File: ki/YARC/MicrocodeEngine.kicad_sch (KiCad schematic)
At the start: 12 parts, among them U32 74HC245, U33 AS6C6264, U34 74LS574, U35 74HC245, U36 AS6C6264, U37 74LS574, U38 74HC245, U39 AS6C6264, U40 74LS574, U41 74HC245, U42 AS6C6264, U43 74LS574

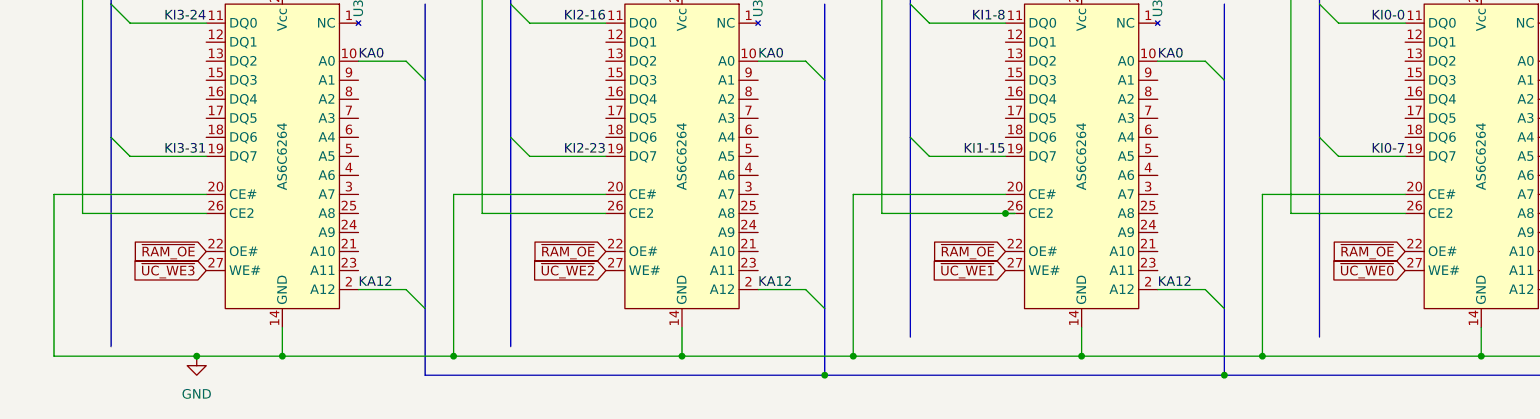
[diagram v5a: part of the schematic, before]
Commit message: Large commit. Document two hardware changes to microcode controls. Adapt Nano firmware to these changes. Significantly simplify initialization logic and make it more consistent about reset.
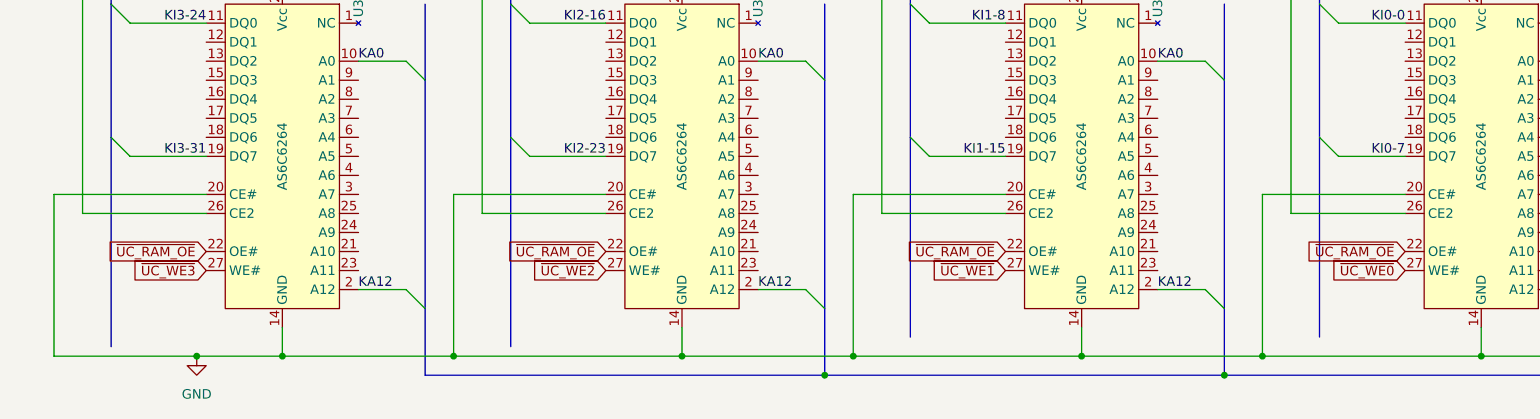
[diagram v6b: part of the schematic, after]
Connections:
- net ~{RAM_OE} renamed ~{UC_RAM_OE}
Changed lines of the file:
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@@
   (junction (at 205.74 165.1) (diameter 0) (color 0 0 0 0)
   )
-  (junction (at 142.24 146.05) (diameter 0) (color 0 0 0 0)
-  )
   (junction (at 45.72 165.1) (diameter 0) (color 0 0 0 0)
   )
@@
     (stroke (width 0) (type default) (color 0 0 0 0))
   )
+  (wire (pts (xy 125.73 146.05) (xy 142.24 146.05))
+    (stroke (width 0) (type default) (color 0 0 0 0))
+  )
   (bus (pts (xy 184.15 62.23) (xy 184.15 72.39))
     (stroke (width 0) (type default) (color 0 0 0 0))
@@
     (stroke (width 0) (type default) (color 0 0 0 0))
   )
-  (wire (pts (xy 142.24 146.05) (xy 125.73 146.05))
-    (stroke (width 0) (type default) (color 0 0 0 0))
-  )
   (bus (pts (xy 129.54 62.23) (xy 142.24 62.23))
     (stroke (width 0) (type default) (color 0 0 0 0))
@@
     (stroke (width 0) (type default) (color 0 0 0 0))
   )
-  (wire (pts (xy 143.51 146.05) (xy 142.24 146.05))
-    (stroke (width 0) (type default) (color 0 0 0 0))
-  )
   (wire (pts (xy 152.4 67.31) (xy 99.06 67.31))
     (stroke (width 0) (type default) (color 0 0 0 0))
@@
     )
   )
-  (global_label "~{RAM_OE}" (shape input) (at 35.56 151.13 180) (fields_autoplaced)
-    (effects (font (size 1.27 1.27)) (justify right))
-    (property "Intersheet References" "${INTERSHEET_REFS}" (id 0) (at 25.8898 151.0506 0)
-      (effects (font (size 1.27 1.27)) (justify right) hide)
-    )
-  )
-  (global_label "~{RAM_OE}" (shape input) (at 88.9 151.13 180) (fields_autoplaced)
-    (effects (font (size 1.27 1.27)) (justify right))
-    (property "Intersheet References" "${INTERSHEET_REFS}" (id 0) (at 79.2298 151.0506 0)
+  (global_label "~{UC_RAM_OE}" (shape input) (at 35.56 151.13 180) (fields_autoplaced)
+    (effects (font (size 1.27 1.27)) (justify right))
+    (property "Intersheet References" "${INTERSHEET_REFS}" (id 0) (at 22.3217 151.2094 0)
+      (effects (font (size 1.27 1.27)) (justify right) hide)
+    )
+  )
+  (global_label "~{UC_RAM_OE}" (shape input) (at 195.58 151.13 180) (fields_autoplaced)
+    (effects (font (size 1.27 1.27)) (justify right))
+    (property "Intersheet References" "${INTERSHEET_REFS}" (id 0) (at 182.3417 151.2094 0)
       (effects (font (size 1.27 1.27)) (justify right) hide)
     )
@@
     )
   )
-  (global_label "~{RAM_OE}" (shape input) (at 142.24 151.13 180) (fields_autoplaced)
-    (effects (font (size 1.27 1.27)) (justify right))
-    (property "Intersheet References" "${INTERSHEET_REFS}" (id 0) (at 132.5698 151.0506 0)
-      (effects (font (size 1.27 1.27)) (justify right) hide)
-    )
-  )
-  (global_label "~{RAM_OE}" (shape input) (at 195.58 151.13 180) (fields_autoplaced)
-    (effects (font (size 1.27 1.27)) (justify right))
-    (property "Intersheet References" "${INTERSHEET_REFS}" (id 0) (at 185.9098 151.0506 0)
+  (global_label "~{UC_RAM_OE}" (shape input) (at 88.9 151.13 180) (fields_autoplaced)
+    (effects (font (size 1.27 1.27)) (justify right))
+    (property "Intersheet References" "${INTERSHEET_REFS}" (id 0) (at 75.6617 151.2094 0)
       (effects (font (size 1.27 1.27)) (justify right) hide)
     )
@@
       (effects (font (size 1.27 1.27)) (justify right) hide)
     )
+  )
+  (global_label "~{UC_RAM_OE}" (shape input) (at 142.24 151.13 180) (fields_autoplaced)
+    (effects (font (size 1.27 1.27)) (justify right))
+    (property "Intersheet References" "${INTERSHEET_REFS}" (id 0) (at 129.0017 151.2094 0)
+      (effects (font (size 1.27 1.27)) (justify right) hide)
+    )

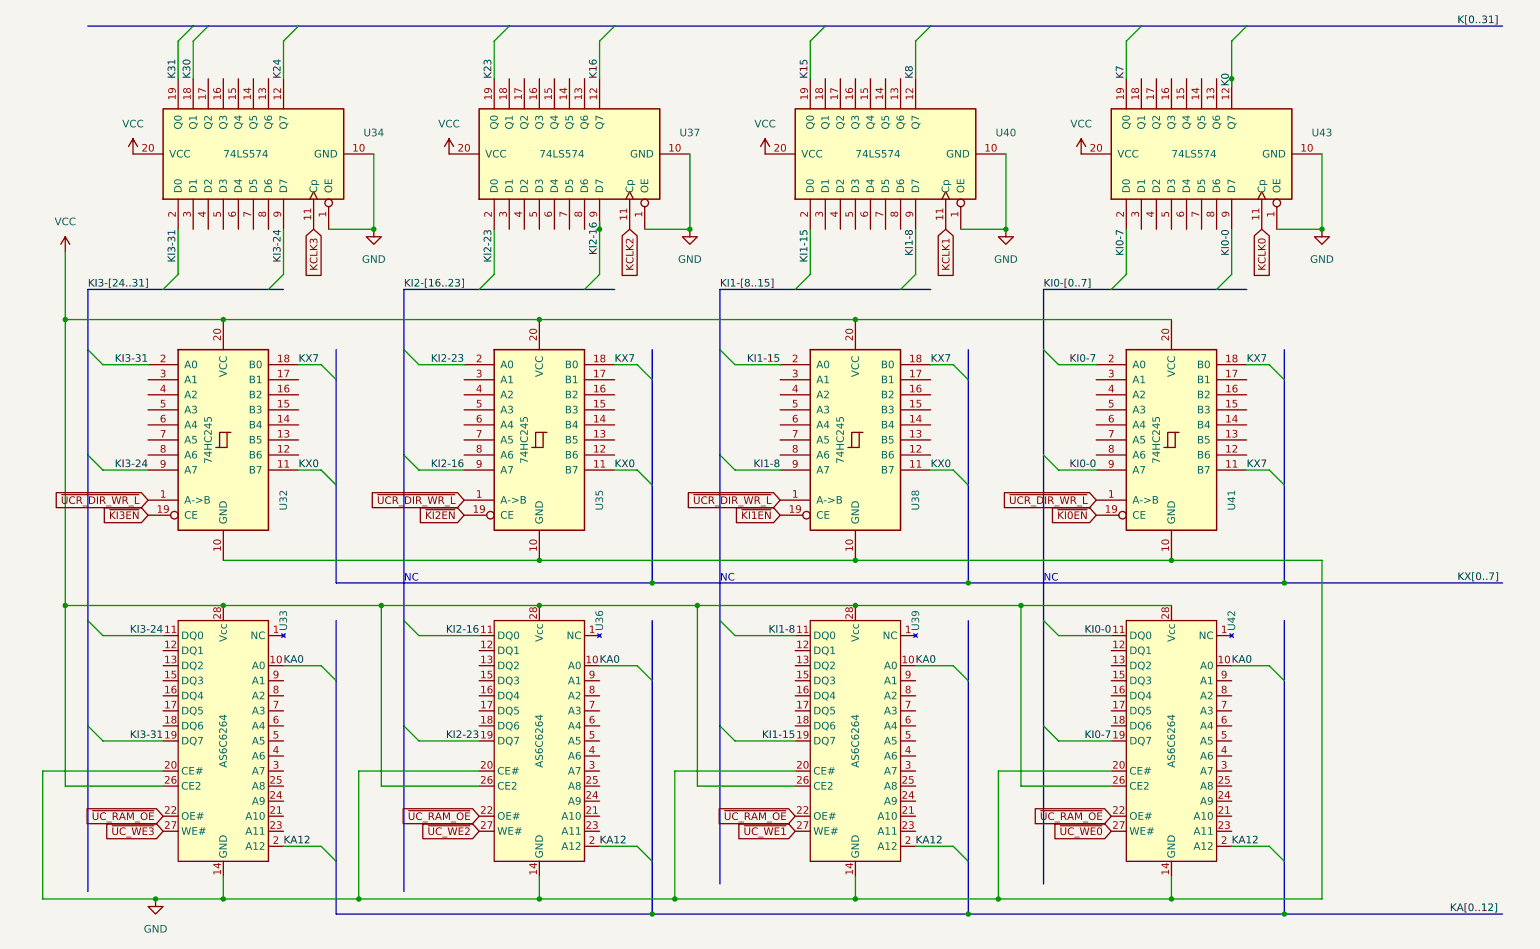
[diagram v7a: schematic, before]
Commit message: Removed about 2/3 of 2300+ errors from the ERC
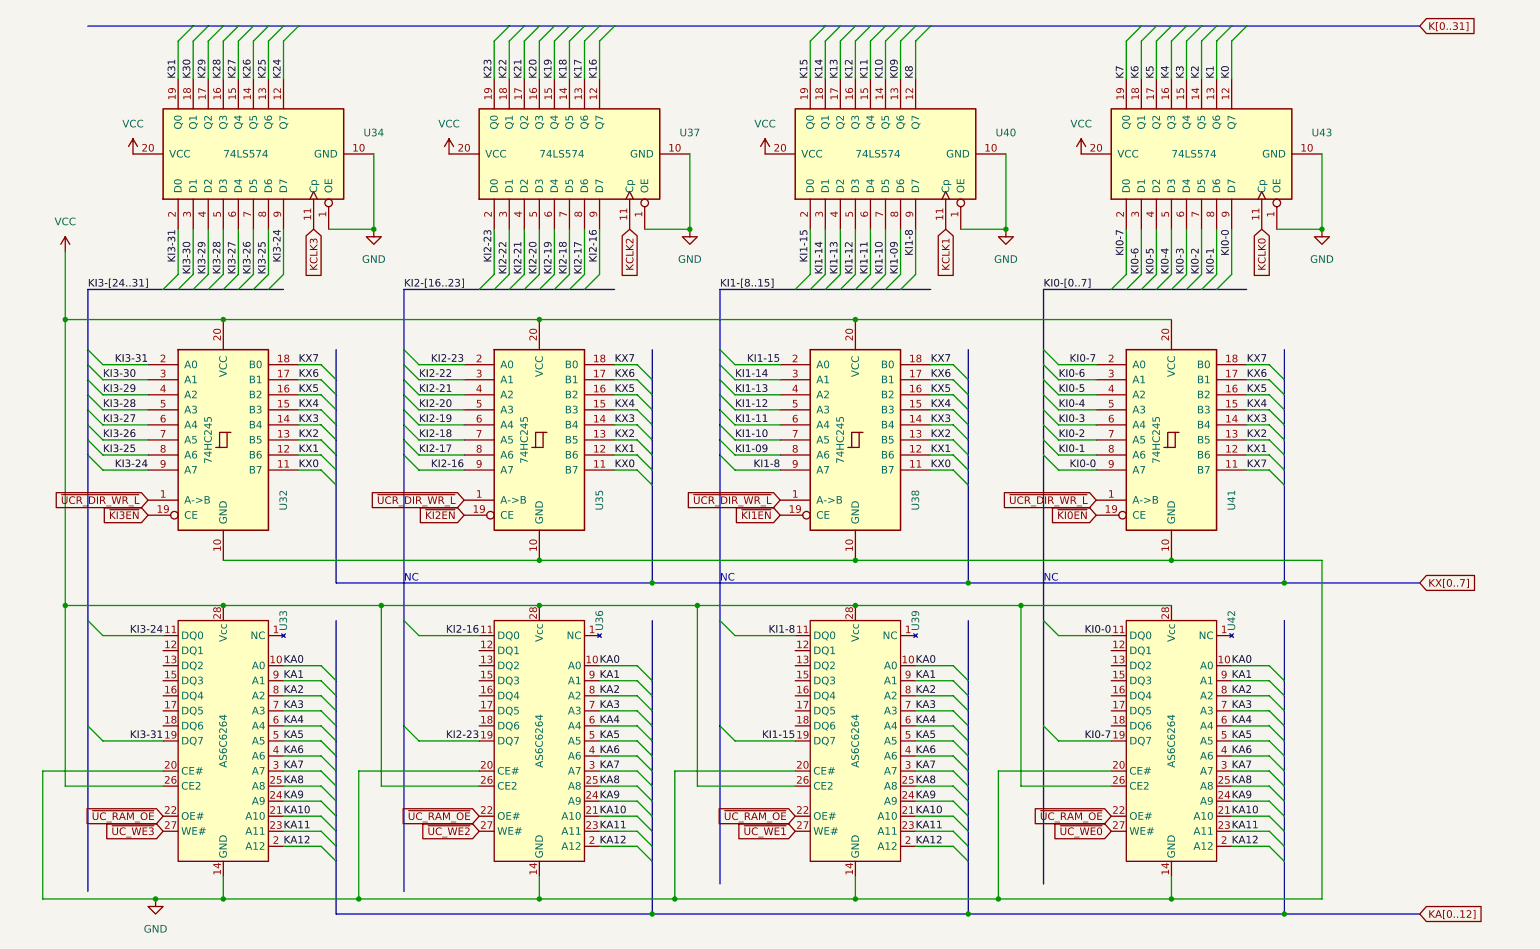
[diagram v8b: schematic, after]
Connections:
- net K17: now reaches U37.13 (Q6)
- net K18: now reaches U37.14 (Q5)
- net K19: now reaches U37.15 (Q4)
- net K20: now reaches U37.16 (Q3)
- net K21: now reaches U37.17 (Q2)
- net K22: now reaches U37.18 (Q1)
- net KI2-22: now reaches U37.3 (D1)
- net KI2-22: now also U35.3 (A1)
- net KI2-21: now reaches U37.4 (D2)
- net KI2-21: now also U35.4 (A2)
- net KI2-20: now reaches U37.5 (D3)
- net KI2-20: now also U35.5 (A3)
- net KI2-19: now reaches U37.6 (D4)
- net KI2-19: now also U35.6 (A4)
- net KI2-18: now reaches U37.7 (D5)
- net KI2-18: now also U35.7 (A5)
- net KI2-17: now reaches U37.8 (D6)
- net KI2-17: now also U35.8 (A6)
- net KA10: now reaches U36.21 (A10)
- net KA10: now also U33.21 (A10), U39.21 (A10), U42.21 (A10)
- net KA11: now reaches U36.23 (A11)
- net KA11: now also U33.23 (A11), U39.23 (A11), U42.23 (A11)
- net KA9: now reaches U36.24 (A9)
- net KA9: now also U33.24 (A9), U39.24 (A9), U42.24 (A9)
- net KA8: now reaches U36.25 (A8)
- net KA8: now also U33.25 (A8), U39.25 (A8), U42.25 (A8)
- net KA7: now reaches U36.3 (A7)
- net KA7: now also U33.3 (A7), U39.3 (A7), U42.3 (A7)
- net KA6: now reaches U36.4 (A6)
- net KA6: now also U33.4 (A6), U39.4 (A6), U42.4 (A6)
- net KA5: now reaches U36.5 (A5)
- net KA5: now also U33.5 (A5), U39.5 (A5), U42.5 (A5)
- net KA4: now reaches U36.6 (A4)
- net KA4: now also U33.6 (A4), U39.6 (A4), U42.6 (A4)
- net KA3: now reaches U36.7 (A3)
- net KA3: now also U33.7 (A3), U39.7 (A3), U42.7 (A3)
- net KA2: now reaches U36.8 (A2)
- net KA2: now also U33.8 (A2), U39.8 (A2), U42.8 (A2)
- net KA1: now reaches U36.9 (A1)
- net KA1: now also U33.9 (A1), U39.9 (A1), U42.9 (A1)
- net KX1: now reaches U32.12 (B6)
- net KX1: now also U35.12 (B6), U38.12 (B6), U41.12 (B6)
- net KX2: now reaches U32.13 (B5)
- net KX2: now also U35.13 (B5), U38.13 (B5), U41.13 (B5)
- net KX3: now reaches U32.14 (B4)
- net KX3: now also U35.14 (B4), U38.14 (B4), U41.14 (B4)
- net KX4: now reaches U32.15 (B3)
- net KX4: now also U35.15 (B3), U38.15 (B3), U41.15 (B3)
- net KX5: now reaches U32.16 (B2)
- net KX5: now also U35.16 (B2), U38.16 (B2), U41.16 (B2)
- net KX6: now reaches U32.17 (B1)
- net KX6: now also U35.17 (B1), U38.17 (B1), U41.17 (B1)
- net KI3-30: now reaches U32.3 (A1)
- net KI3-30: now also U34.3 (D1)
- net KI3-29: now reaches U32.4 (A2)
- net KI3-29: now also U34.4 (D2)
- net KI3-28: now reaches U32.5 (A3)
- net KI3-28: now also U34.5 (D3)
- net KI3-27: now reaches U32.6 (A4)
- net KI3-27: now also U34.6 (D4)
- net KI3-26: now reaches U32.7 (A5)
- net KI3-26: now also U34.7 (D5)
- net KI3-25: now reaches U32.8 (A6)
- net KI3-25: now also U34.8 (D6)
- net K1: now reaches U43.13 (Q6)
- net K2: now reaches U43.14 (Q5)
- net K3: now reaches U43.15 (Q4)
- net K4: now reaches U43.16 (Q3)
- net K5: now reaches U43.17 (Q2)
- net K6: now reaches U43.18 (Q1)
- net KI0-6: now reaches U43.3 (D1)
- net KI0-6: now also U41.3 (A1)
- net KI0-5: now reaches U43.4 (D2)
- net KI0-5: now also U41.4 (A2)
- net KI0-4: now reaches U43.5 (D3)
- net KI0-4: now also U41.5 (A3)
- net KI0-3: now reaches U43.6 (D4)
- net KI0-3: now also U41.6 (A4)
- net KI0-2: now reaches U43.7 (D5)
- net KI0-2: now also U41.7 (A5)
- net KI0-1: now reaches U43.8 (D6)
- net KI0-1: now also U41.8 (A6)
- net K25: now reaches U34.13 (Q6)
- net K26: now reaches U34.14 (Q5)
- net K27: now reaches U34.15 (Q4)
- net K28: now reaches U34.16 (Q3)
- net K29: now reaches U34.17 (Q2)
- net K09: now reaches U40.13 (Q6)
- net K10: now reaches U40.14 (Q5)
- net K11: now reaches U40.15 (Q4)
- net K12: now reaches U40.16 (Q3)
- net K13: now reaches U40.17 (Q2)
- net K14: now reaches U40.18 (Q1)
- net KI1-14: now reaches U40.3 (D1)
- net KI1-14: now also U38.3 (A1)
- net KI1-13: now reaches U40.4 (D2)
- net KI1-13: now also U38.4 (A2)
- net KI1-12: now reaches U40.5 (D3)
- net KI1-12: now also U38.5 (A3)
- net KI1-11: now reaches U40.6 (D4)
- net KI1-11: now also U38.6 (A4)
- net KI1-10: now reaches U40.7 (D5)
- net KI1-10: now also U38.7 (A5)
- net KI1-09: now reaches U40.8 (D6)
- net KI1-09: now also U38.8 (A6)
